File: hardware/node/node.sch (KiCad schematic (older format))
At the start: 69 parts, among them J1 BOOT0_Jumper, J2 FTDI, J3 SMA Female, J4 2 x AA, J5 SWD, Q1 Si2323DDS, SW1 TVCM04N016BB, U1 RFM69HCW, U2 SHTC3, U3 AT25DF512C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

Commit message: Change to RFM69HW
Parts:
- U1: value RFM69HCW -> RFM69HW; footprint humidity:RFM69HCW -> humidity:RFM69HW; symbol RF_AM_FM:RFM69HCW -> humidity:RFM69HW
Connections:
- net ANT: now also U1.10 (ANT); no longer U1.9 (ANT)
- net CS_FLASH: now also U4.15 (PB1); no longer U4.14 (PB0)
- net CS_RFM69: now also U1.15 (NSS), U4.14 (PB0); no longer U1.5 (NSS), U4.15 (PB1)
- net GND: now also U1.11 (GND), U1.9 (GND); no longer U1.1 (GND), U1.10 (GND), U1.8 (GND)
- net RFM69_INT: now also U1.2 (DIO0); no longer U1.14 (DIO0)
- net RFM69_RST: now also U1.1 (RESET); no longer U1.6 (RESET)
- net SPI1_MISO: now also U1.13 (MISO); no longer U1.2 (MISO)
- net SPI1_MOSI: now also U1.14 (MOSI); no longer U1.3 (MOSI)
- net SPI1_SCK: now also U1.12 (SCK); no longer U1.4 (SCK)
- net VCC: now also U1.8 (3.3V); no longer U1.13 (3.3V)
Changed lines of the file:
@@
-$EndComp
-$Comp
-L RF_AM_FM:RFM69HCW U1
-U 1 1 5CD803DB
-P 3900 2050
-F 0 "U1" H 4150 1450 50  0000 C CNN
-F 1 "RFM69HCW" H 3500 1450 50  0000 C CNN
-F 2 "humidity:RFM69HCW" H 600 3700 50  0001 C CNN
-F 3 "http://www.hoperf.com/upload/rf/RFM69HCW-V1.1.pdf" H 600 3700 50  0001 C CNN
-	1    3900 2050
-	1    0    0    -1
 $EndComp
 $Comp
@@
 L power:GND #PWR016
 U 1 1 5CD831AE
-P 4000 2750
-F 0 "#PWR016" H 4000 2500 50  0001 C CNN
-F 1 "GND" H 4005 2577 50  0000 C CNN
-F 2 "" H 4000 2750 50  0001 C CNN
-F 3 "" H 4000 2750 50  0001 C CNN
-	1    4000 2750
+P 3900 2750
+F 0 "#PWR016" H 3900 2500 50  0001 C CNN
+F 1 "GND" H 3905 2577 50  0000 C CNN
+F 2 "" H 3900 2750 50  0001 C CNN
+F 3 "" H 3900 2750 50  0001 C CNN
+	1    3900 2750
 	1    0    0    -1
 $EndComp
@@
 	3800 2700 3900 2700
 Wire Wire Line
-	4000 2700 4000 2750
-Wire Wire Line
-	4000 2700 4000 2650
-Connection ~ 4000 2700
-Wire Wire Line
 	3900 2650 3900 2700
-Connection ~ 3900 2700
-Wire Wire Line
-	3900 2700 4000 2700
 $Comp
 L power:GND #PWR015
@@
 Wire Wire Line
 	1050 2600 550  2600
+Text Label 550  2600 0    50   ~ 0
+CS_RFM69
+Wire Wire Line
+	1050 2700 550  2700
 Text Label 550  2700 0    50   ~ 0
-CS_RFM69
-Wire Wire Line
-	1050 2700 550  2700
-Text Label 550  2600 0    50   ~ 0
 CS_FLASH
 Wire Wire Line
@@
 Text Label 2750 2800 2    50   ~ 0
 RFM69_RST
+$Comp
+L humidity:RFM69HW U1
+U 1 1 5CD803DB
+P 3900 2050
+F 0 "U1" H 4150 1450 50  0000 C CNN
+F 1 "RFM69HW" H 3500 1450 50  0000 C CNN
+F 2 "humidity:RFM69HW" H 600 3700 50  0001 C CNN
+F 3 "http://www.hoperf.com/upload/rf/RFM69HCW-V1.1.pdf" H 600 3700 50  0001 C CNN
+	1    3900 2050
+	1    0    0    -1
+$EndComp
+Wire Wire Line
+	3900 2750 3900 2700
+Connection ~ 3900 2700
 $EndSCHEMATC

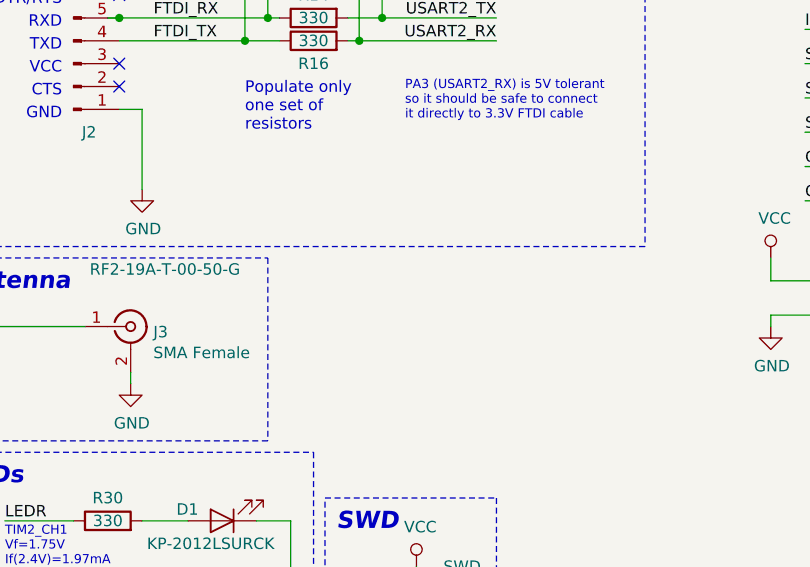
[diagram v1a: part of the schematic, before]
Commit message: Moved mounting holes. Slightly narrower PCB
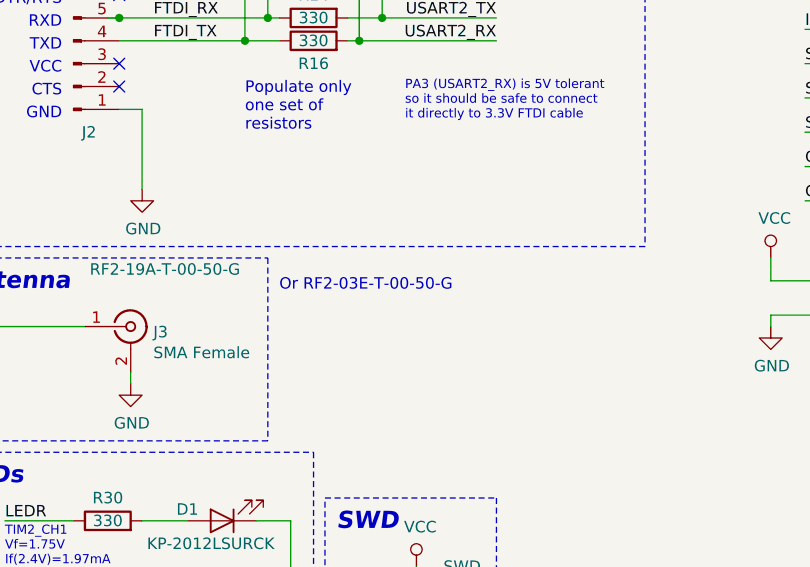
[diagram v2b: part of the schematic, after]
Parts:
- J4: footprint Connector_JST:JST_PH_S3B-PH-K_1x03_P2.00mm_Horizontal -> Connector_PinHeader_2.54mm:PinHeader_1x03_P2.54mm_Vertical
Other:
- note added: "Or RF2-03E-T-00-50-G"
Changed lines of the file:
@@
 F 0 "J4" H 650 7250 50  0000 C CNN
 F 1 "2 x AA" H 650 6900 50  0000 C CNN
-F 2 "Connector_JST:JST_PH_S3B-PH-K_1x03_P2.00mm_Horizontal" H 550 7050 50  0001 C CNN
+F 2 "Connector_PinHeader_2.54mm:PinHeader_1x03_P2.54mm_Vertical" H 550 7050 50  0001 C CNN
 F 3 "~" H 550 7050 50  0001 C CNN
 	1    550  7050
@@
 	3900 2750 3900 2700
 Connection ~ 3900 2700
+Text Notes 5500 5800 0    50   ~ 0
+Or RF2-03E-T-00-50-G
 $EndSCHEMATC

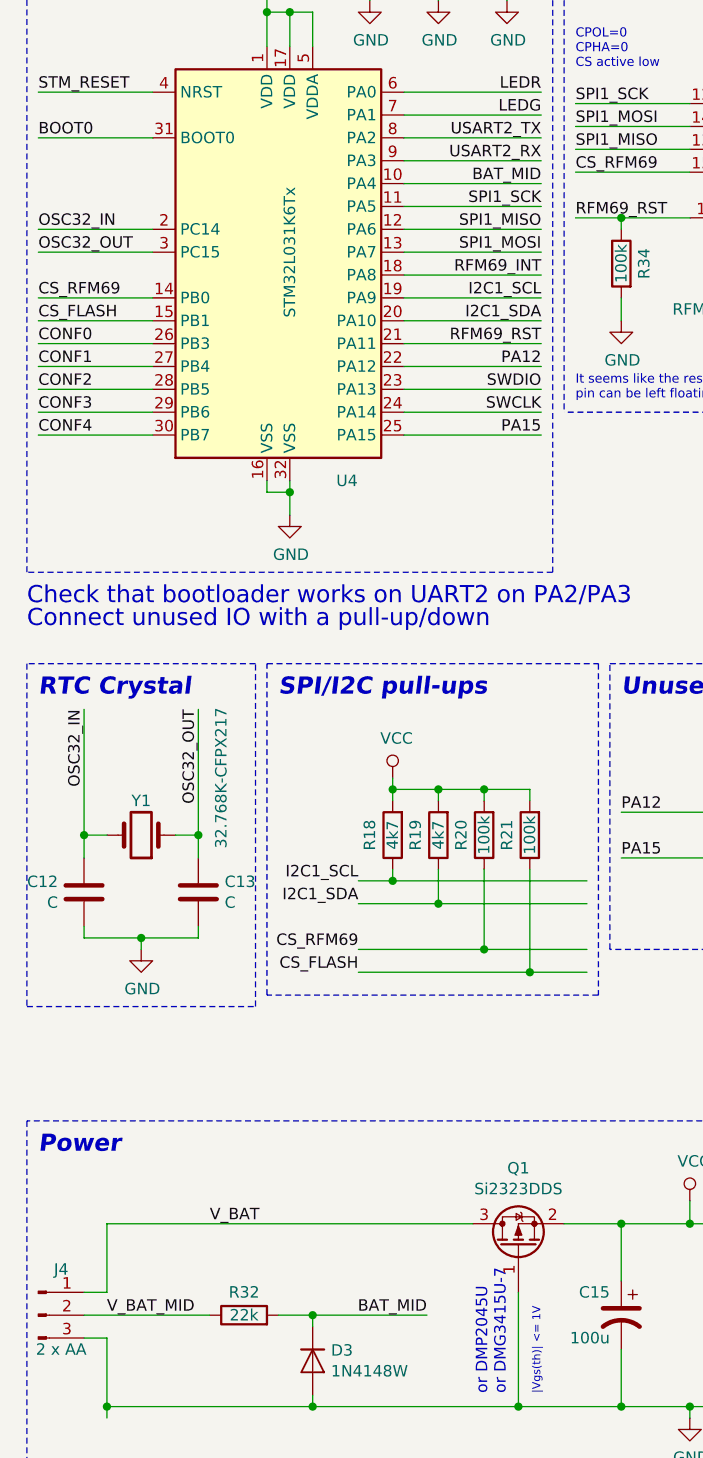
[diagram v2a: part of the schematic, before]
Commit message: Move power connector to other side
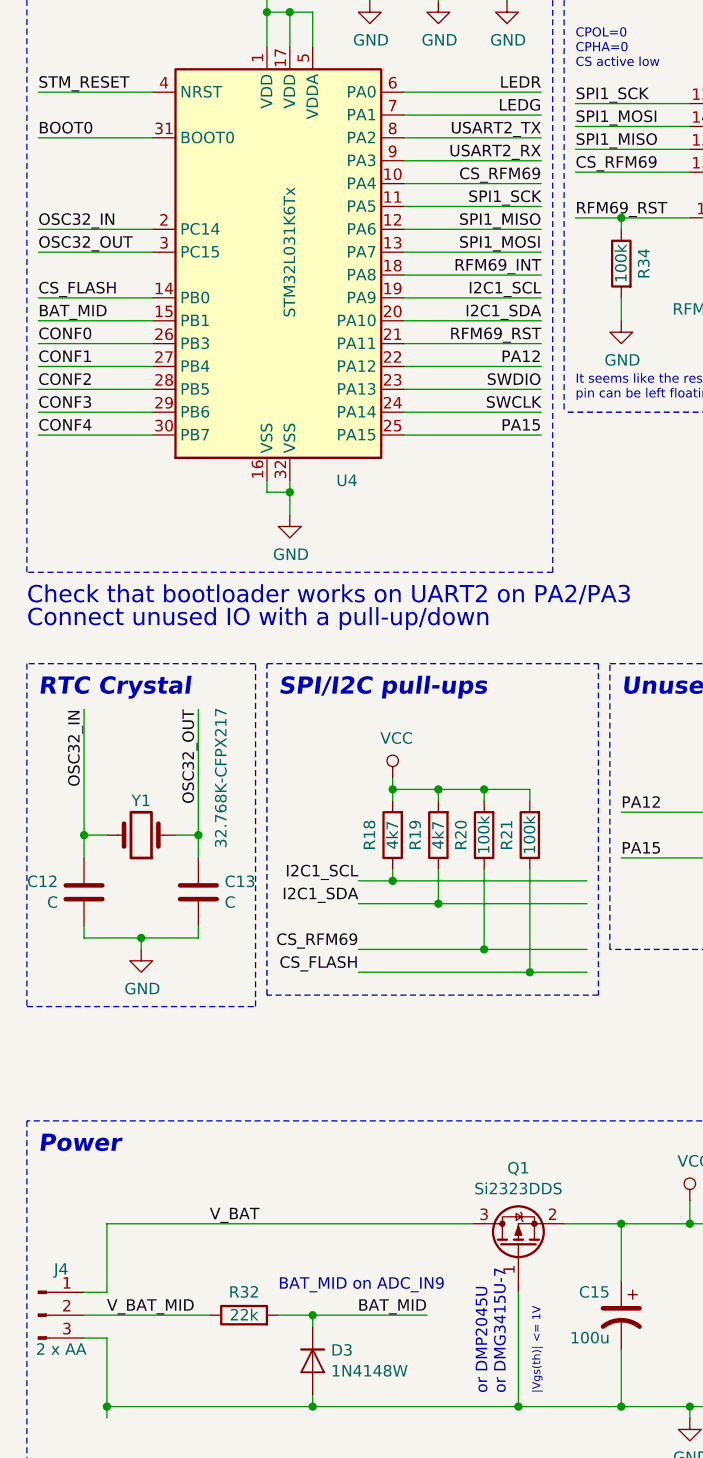
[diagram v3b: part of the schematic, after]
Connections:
- net BAT_MID: now also U4.15 (PB1); no longer U4.10 (PA4)
- net CS_FLASH: now also U4.14 (PB0); no longer U4.15 (PB1)
- net CS_RFM69: now also U4.10 (PA4); no longer U4.14 (PB0)
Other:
- note added: "BAT_MID on ADC_IN9"
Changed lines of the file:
@@
 Wire Wire Line
 	1050 2600 550  2600
+Text Label 2750 2100 2    50   ~ 0
+CS_RFM69
+Wire Wire Line
+	1050 2700 550  2700
 Text Label 550  2600 0    50   ~ 0
-CS_RFM69
-Wire Wire Line
-	1050 2700 550  2700
-Text Label 550  2700 0    50   ~ 0
 CS_FLASH
 Wire Wire Line
@@
 NoConn ~ 4400 2250
 NoConn ~ 4400 2350
-Text Label 2750 2100 2    50   ~ 0
+Text Label 550  2700 0    50   ~ 0
 BAT_MID
 Wire Wire Line
@@
 Text Notes 5500 5800 0    50   ~ 0
 Or RF2-03E-T-00-50-G
+Text Notes 1600 6950 0    50   ~ 0
+BAT_MID on ADC_IN9
 $EndSCHEMATC

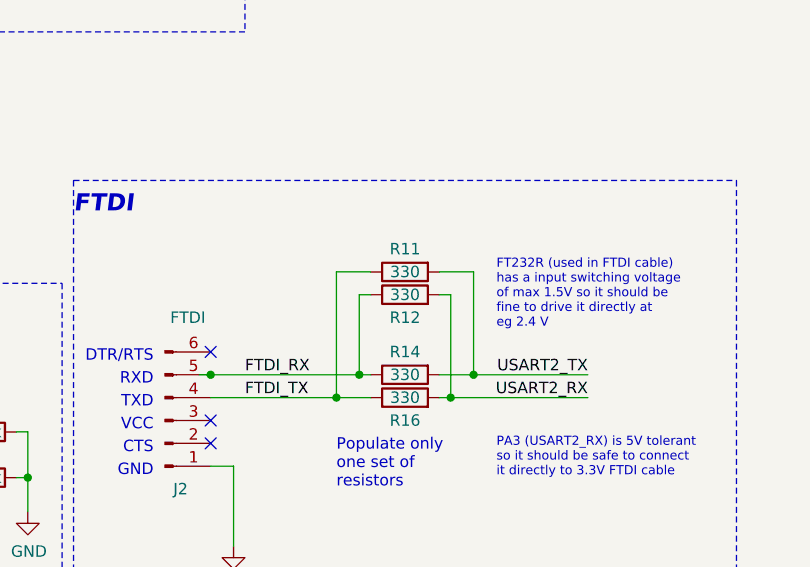
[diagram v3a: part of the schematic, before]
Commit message: Add resistors as DNP
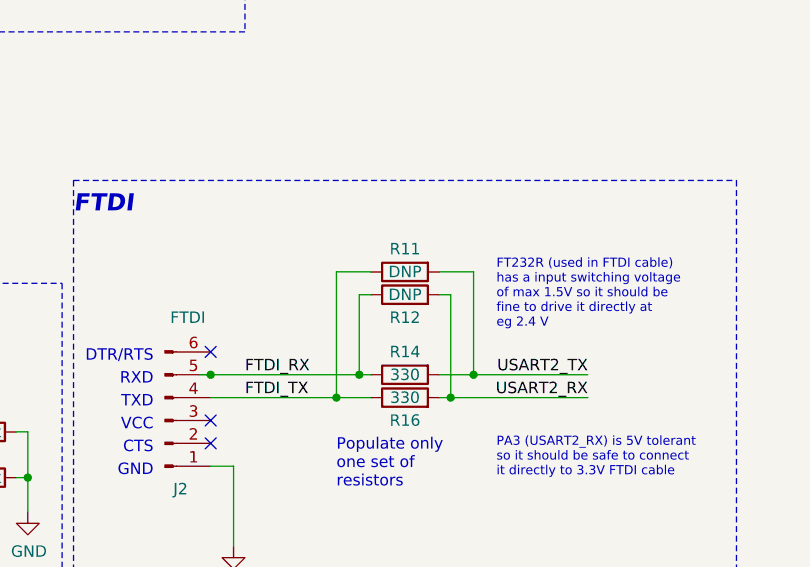
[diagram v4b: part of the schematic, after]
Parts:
- J2: footprint Connector_PinHeader_2.54mm:PinHeader_1x06_P2.54mm_Horizontal -> Connector_PinHeader_2.54mm:PinHeader_1x06_P2.54mm_Vertical
- R11, R12: value 330 -> DNP; footprint Resistor_SMD:R_0603_1608Metric_Pad1.05x0.95mm_HandSolder -> humidity:R_0603_1608Metric_Pad1.05x0.95mm_HandSolder-DNP; DNPValue (none) -> 330
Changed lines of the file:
@@
 F 0 "J2" H 4700 5100 50  0000 R CNN
 F 1 "FTDI" H 4700 4350 50  0000 C CNN
-F 2 "Connector_PinHeader_2.54mm:PinHeader_1x06_P2.54mm_Horizontal" H 4600 4800 50  0001 C CNN
+F 2 "Connector_PinHeader_2.54mm:PinHeader_1x06_P2.54mm_Vertical" H 4600 4800 50  0001 C CNN
 F 3 "~" H 4600 4800 50  0001 C CNN
 	1    4600 4800
@@
 P 5650 4150
 F 0 "R11" V 5550 4150 50  0000 C CNN
-F 1 "330" V 5650 4150 50  0000 C CNN
-F 2 "Resistor_SMD:R_0603_1608Metric_Pad1.05x0.95mm_HandSolder" V 5580 4150 50  0001 C CNN
+F 1 "DNP" V 5650 4150 50  0000 C CNN
+F 2 "humidity:R_0603_1608Metric_Pad1.05x0.95mm_HandSolder-DNP" V 5580 4150 50  0001 C CNN
 F 3 "~" H 5650 4150 50  0001 C CNN
+F 4 "330" V 5650 4150 50  0001 C CNN "DNPValue"
 	1    5650 4150
 	0    -1   1    0
@@
 P 5650 4250
 F 0 "R12" V 5550 4250 50  0000 C CNN
-F 1 "330" V 5650 4250 50  0000 C CNN
-F 2 "Resistor_SMD:R_0603_1608Metric_Pad1.05x0.95mm_HandSolder" V 5580 4250 50  0001 C CNN
+F 1 "DNP" V 5650 4250 50  0000 C CNN
+F 2 "humidity:R_0603_1608Metric_Pad1.05x0.95mm_HandSolder-DNP" V 5580 4250 50  0001 C CNN
 F 3 "~" H 5650 4250 50  0001 C CNN
+F 4 "330" V 5650 4250 50  0001 C CNN "DNPValue"
 	1    5650 4250
 	0    -1   -1   0

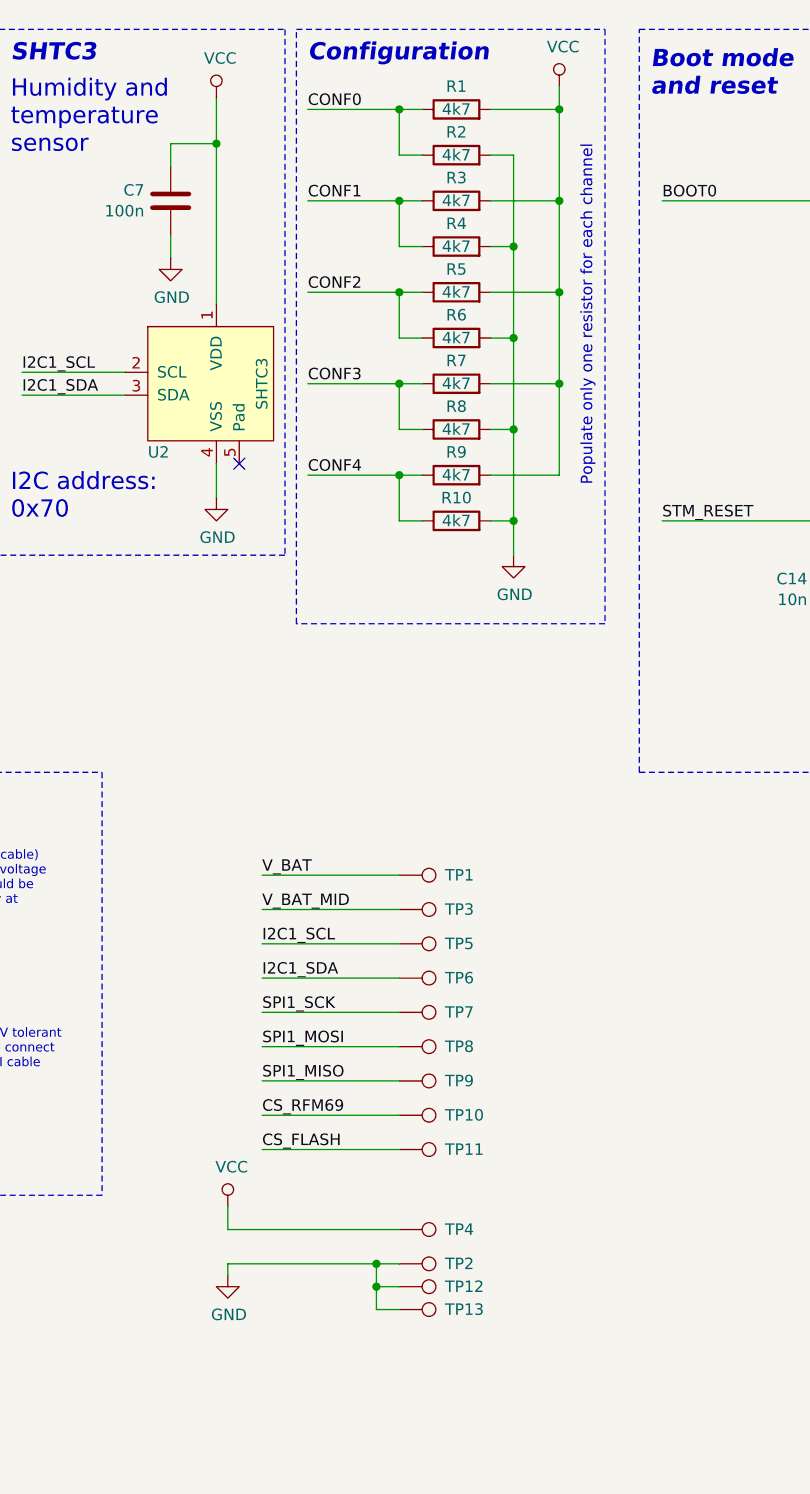
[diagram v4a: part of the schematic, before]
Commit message: Use only resistors to ground to config unit #
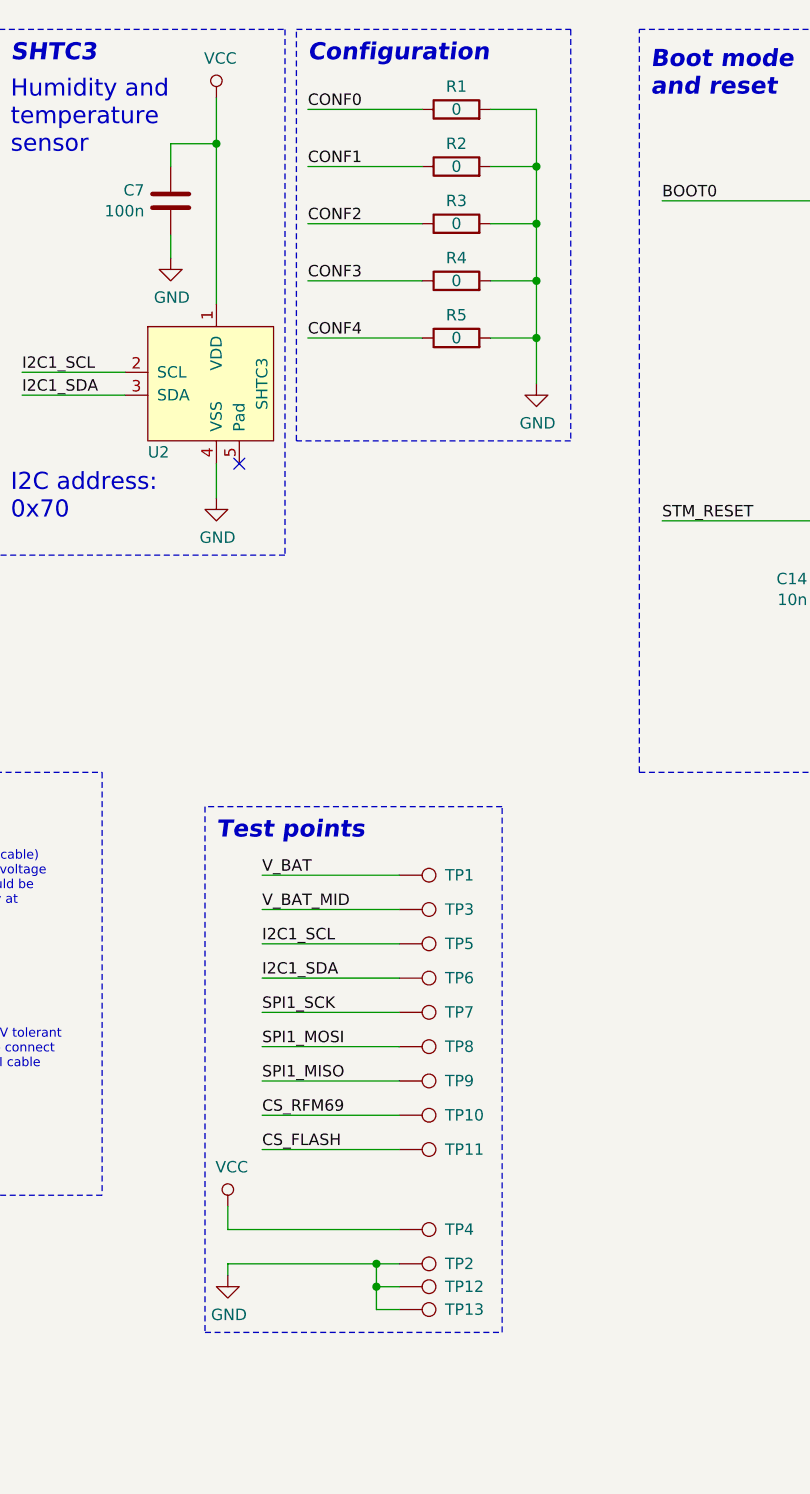
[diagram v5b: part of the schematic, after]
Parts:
- removed R10, R6, R7, R8, R9: 4k7, Resistor_SMD:R_0603_1608Metric_Pad1.05x0.95mm_HandSolder, symbol Device:R
- R1, R2, R3, R4, R5: value 4k7 -> 0
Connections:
- net CONF0: no longer R2.1
- net CONF1: now also R2.1; no longer R3.1, R4.1
- net CONF2: now also R3.1; no longer R5.1
- net CONF3: now also R4.1
- net CONF4: now also R5.1
- net GND: now also R1.2, R3.2, R5.2
- net VCC: no longer R1.2, R3.2, R5.2
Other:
- note added: "Test points"
- note removed: "Populate only one resistor for each channel"
- moved on the sheet: R2, R3, R4, R5

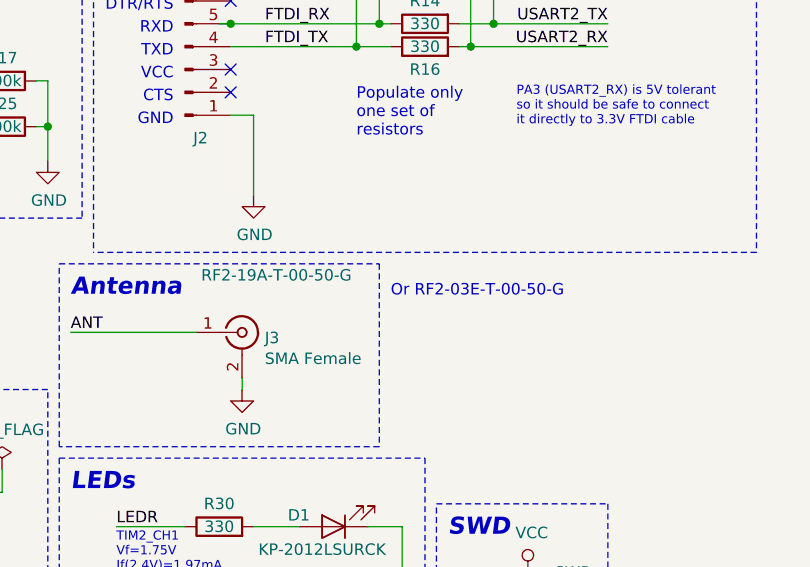
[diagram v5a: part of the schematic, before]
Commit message: Update SMA connector part number
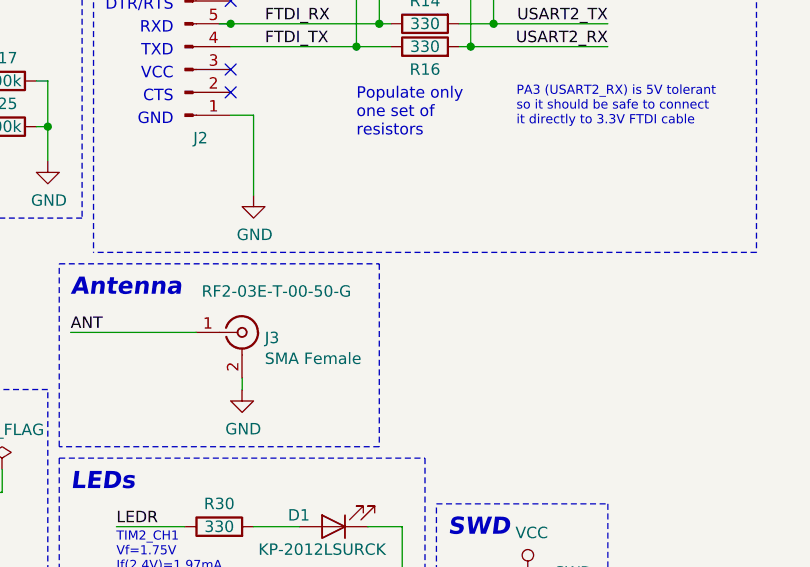
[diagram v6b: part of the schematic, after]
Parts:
- J3: Part RF2-19A-T-00-50-G -> RF2-03E-T-00-50-G
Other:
- note removed: "Or RF2-03E-T-00-50-G"
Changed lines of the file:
@@
 F 2 "humidity:Adam_Tech_SMA_Female_RF2-19A" H 4850 5950 50  0001 C CNN
 F 3 "https://www.tme.eu/Document/bd1bc003b249b3f9362db618e35fe545/RF2-19A-T-00-50-G.pdf" H 4850 5950 50  0001 C CNN
-F 4 "RF2-19A-T-00-50-G" H 5000 6200 50  0000 C CNN "Part"
+F 4 "RF2-03E-T-00-50-G" H 5000 6100 50  0000 C BNN "Part"
 	1    4850 5950
 	1    0    0    -1
@@
 	3900 2750 3900 2700
 Connection ~ 3900 2700
-Text Notes 5500 5800 0    50   ~ 0
-Or RF2-03E-T-00-50-G
 Text Notes 1600 6950 0    50   ~ 0
 BAT_MID on ADC_IN9
